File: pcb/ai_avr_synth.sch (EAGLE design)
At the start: 50 parts, among them IC1 ATMEGA328P-PDIP, J1 1X02ST, J2 1X06, J3 1X08, J4 1X08, J5 MIDIJACK, U1 MC7805, U2 TLC2262, U3 6N138

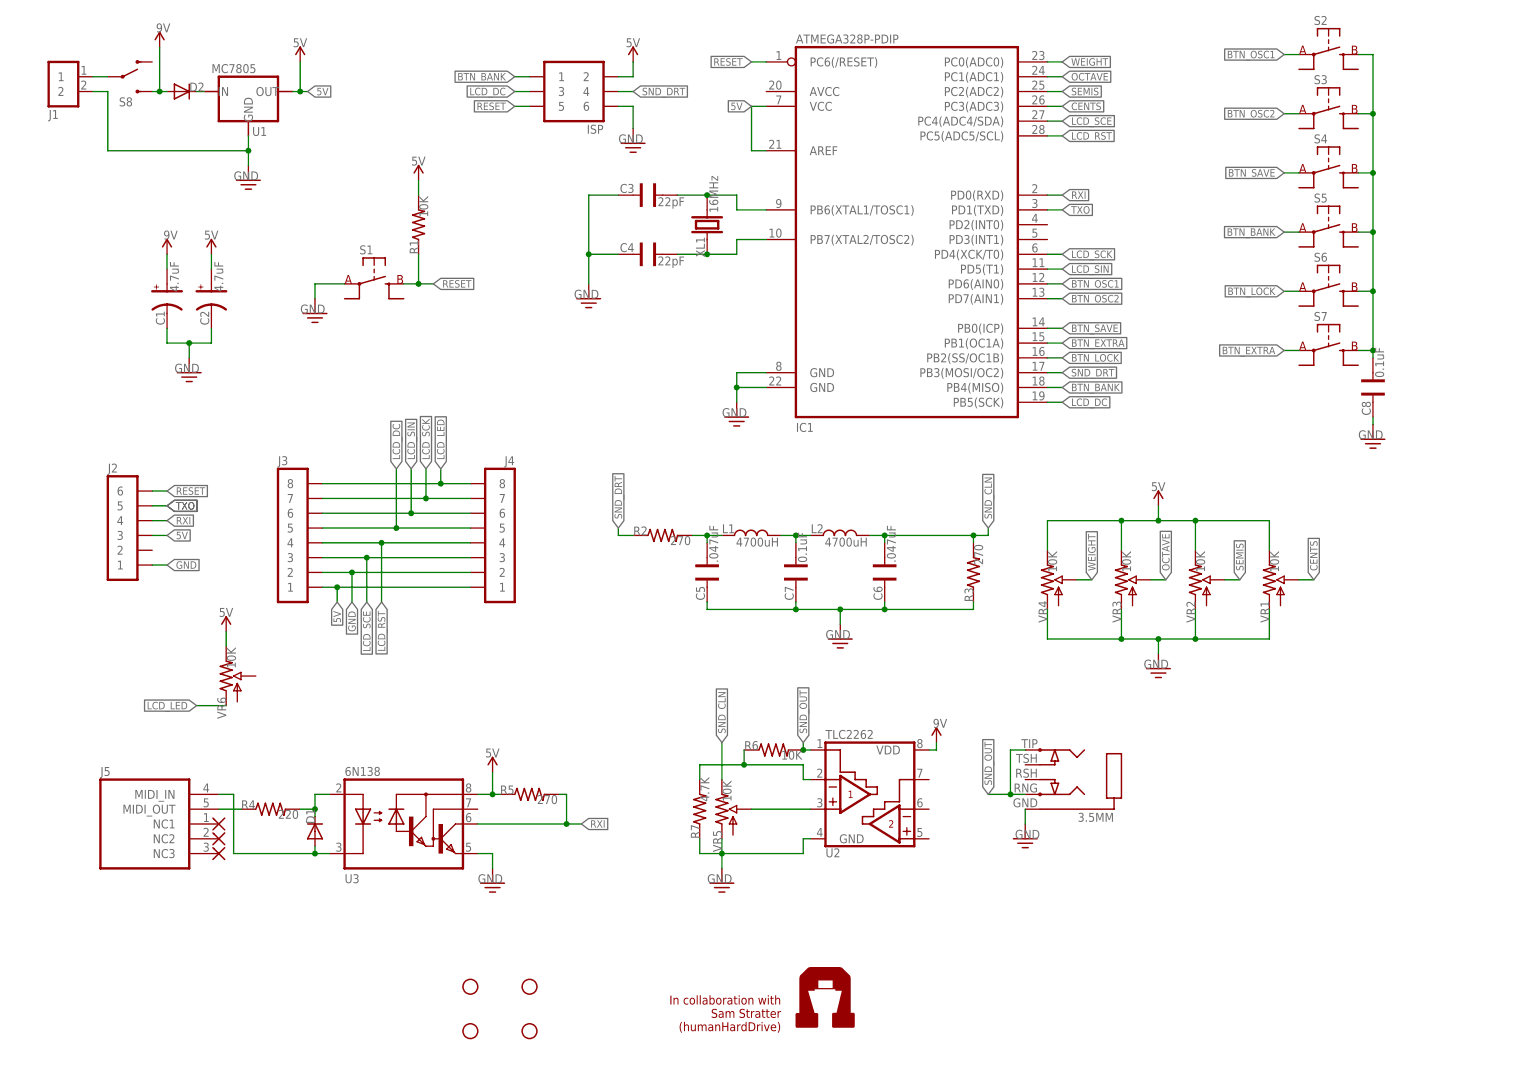
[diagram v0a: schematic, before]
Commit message: updated a few components
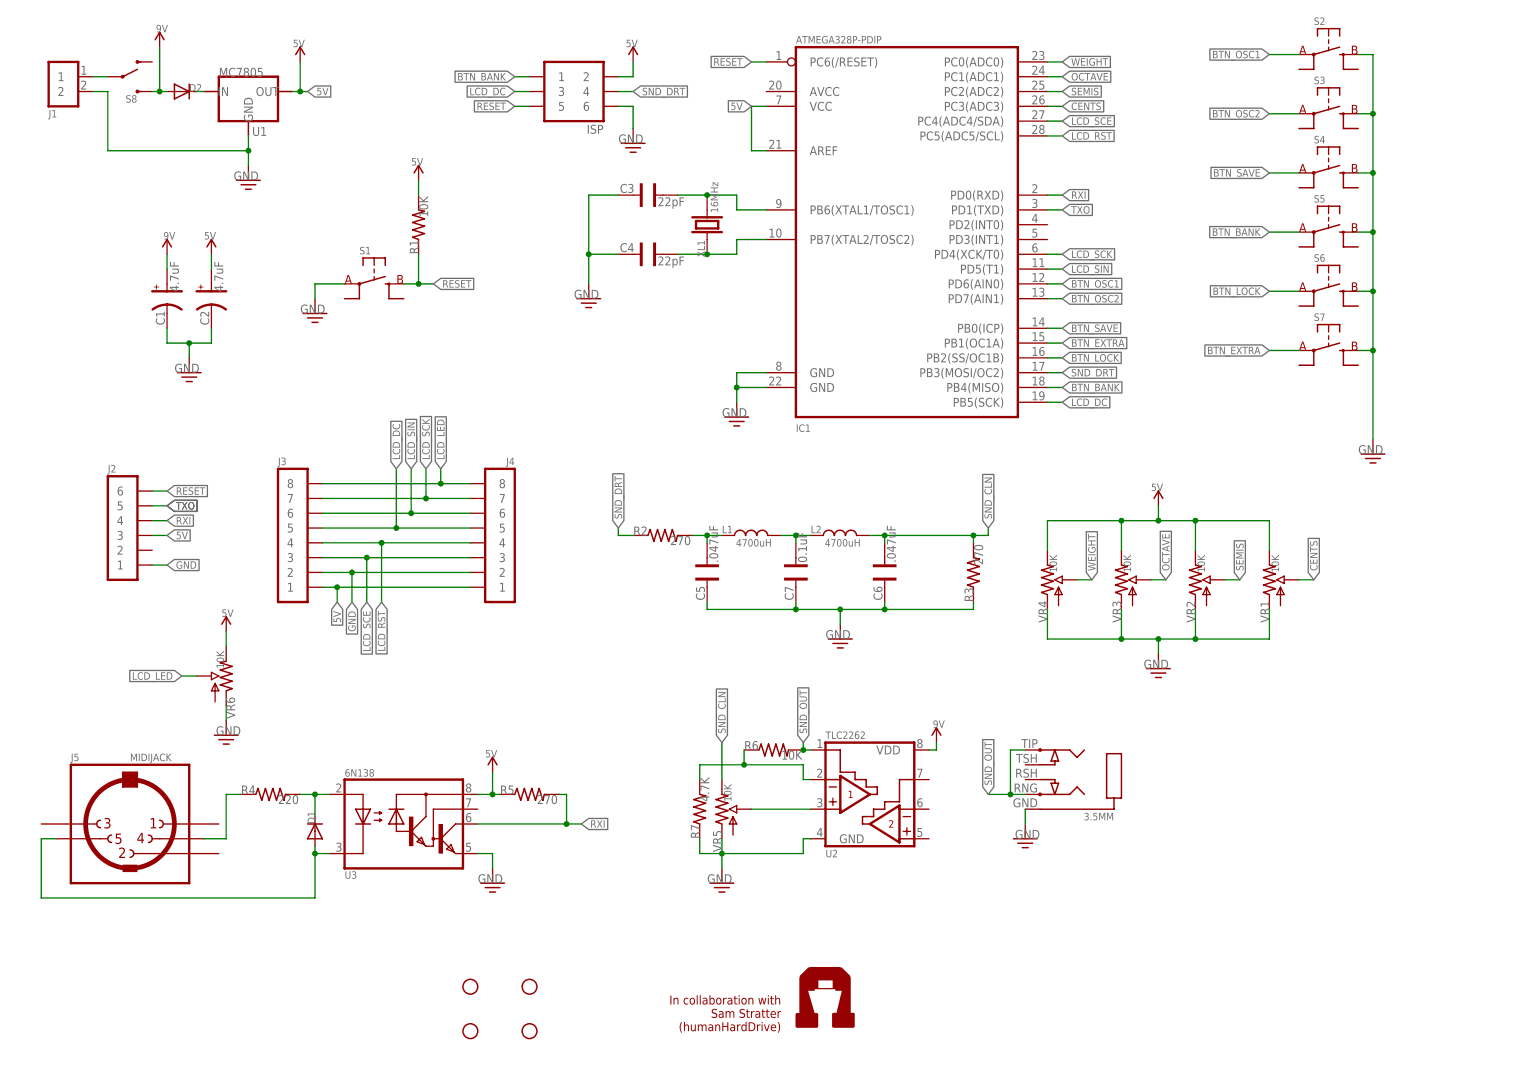
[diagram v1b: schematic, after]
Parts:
- removed C8: 0.1uF, Ai_Passives:CAP025X050
- XL1: device Ai_Passives:CRYSTALHC49S -> Ai_FrequencyControl:CRYSTALHC49S
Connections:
- removed net N$2: C8.1, S2.B@1, S3.B@1, S4.B@1, S5.B@1, S6.B@1, S7.B@1
- net GND: now also S2.B@1, S3.B@1, S4.B@1, S5.B@1, S6.B@1, S7.B@1, VR6.A; no longer C8.2
- net LCD_LED: now also VR6.S; no longer VR6.A
- net N$1: now also J5.4; no longer J5.MIDI_OUT
- net N$10: now also J5.5; no longer J5.MIDI_IN
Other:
- moved on the sheet: R4, VR6

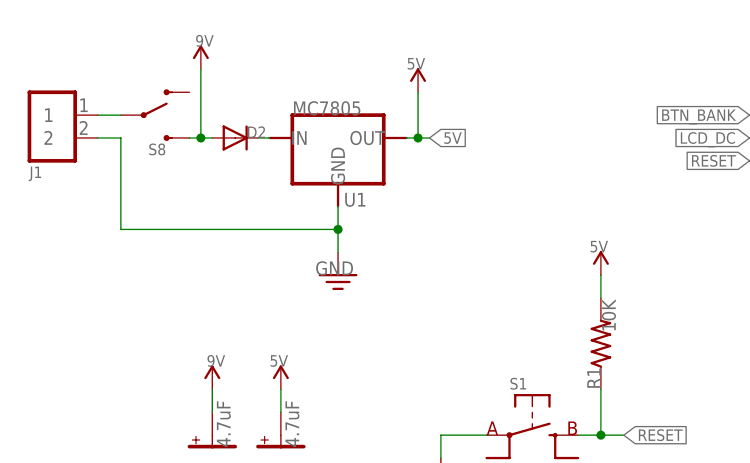
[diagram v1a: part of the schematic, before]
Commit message: fixed trimmer footprint
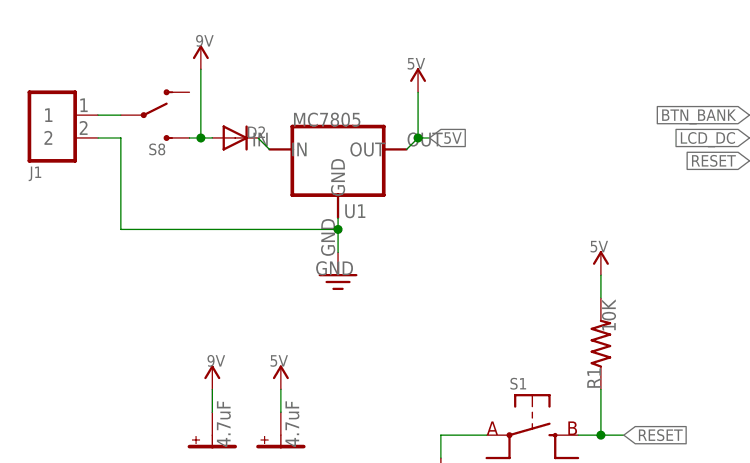
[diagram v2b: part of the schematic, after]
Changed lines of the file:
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@@
 <pinref part="GND1" gate="GND" pin="GND"/>
 <wire x1="40.64" y1="153.67" x2="40.64" y2="156.21" width="0.1524" layer="91"/>
-<wire x1="40.64" y1="156.21" x2="40.64" y2="158.75" width="0.1524" layer="91"/>
+<wire x1="40.64" y1="156.21" x2="40.64" y2="157.48" width="0.1524" layer="91"/>
 <wire x1="16.51" y1="156.21" x2="40.64" y2="156.21" width="0.1524" layer="91"/>
 <junction x="40.64" y="156.21"/>
@@
 <segment>
 <pinref part="U1" gate="G$1" pin="OUT"/>
-<wire x1="48.26" y1="166.37" x2="49.53" y2="166.37" width="0.1524" layer="91"/>
+<wire x1="48.26" y1="165.1" x2="49.53" y2="166.37" width="0.1524" layer="91"/>
 <wire x1="49.53" y1="166.37" x2="49.53" y2="171.45" width="0.1524" layer="91"/>
 <pinref part="U$2" gate="G$1" pin="5V"/>
@@
 <pinref part="D2" gate="G$1" pin="C"/>
 <pinref part="U1" gate="G$1" pin="IN"/>
-<wire x1="31.75" y1="166.37" x2="33.02" y2="166.37" width="0.1524" layer="91"/>
-</segment>
-</net>
+<wire x1="31.75" y1="166.37" x2="33.02" y2="165.1" width="0.1524" layer="91"/>
+</segment>
+</net>

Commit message: updating
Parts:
- removed J2: 1X06, Ai_Connectors:1X06
- added FTDI: 1X06, Ai_Connectors:1X06
- D1: value (none) -> 1N4148
- D2: value (none) -> 1N4001
- STANDOFF5, STANDOFF6, STANDOFF7, STANDOFF8: value STAND-OFF -> STAND-OFF4; device Ai_Electromechanical:STAND-OFF -> Ai_Electromechanical:STAND-OFF4
- U$5: value AI-LOGOL -> AI-LOGOXS; device Ai_Miscellany:AI-LOGOL -> Ai_Miscellany:AI-LOGOXS
- U1: value MC7805 -> MC7805-HOR; device Ai_Power:MC7805 -> Ai_Power:MC7805-HOR
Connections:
- net 5V: now also FTDI.3; no longer J2.3
- net GND: now also FTDI.1; no longer J2.1
- net RESET: now also FTDI.6; no longer J2.6
- net RXI: now also FTDI.4; no longer J2.4
- net TXO: now also FTDI.5; no longer J2.5
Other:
- note removed: "In collaboration with Sam Stratter (humanHardDrive)"
- moved on the sheet: 3.5MM, C1, C2, C3, C4, C5, C6, C7, D1, D2, ISP, J1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

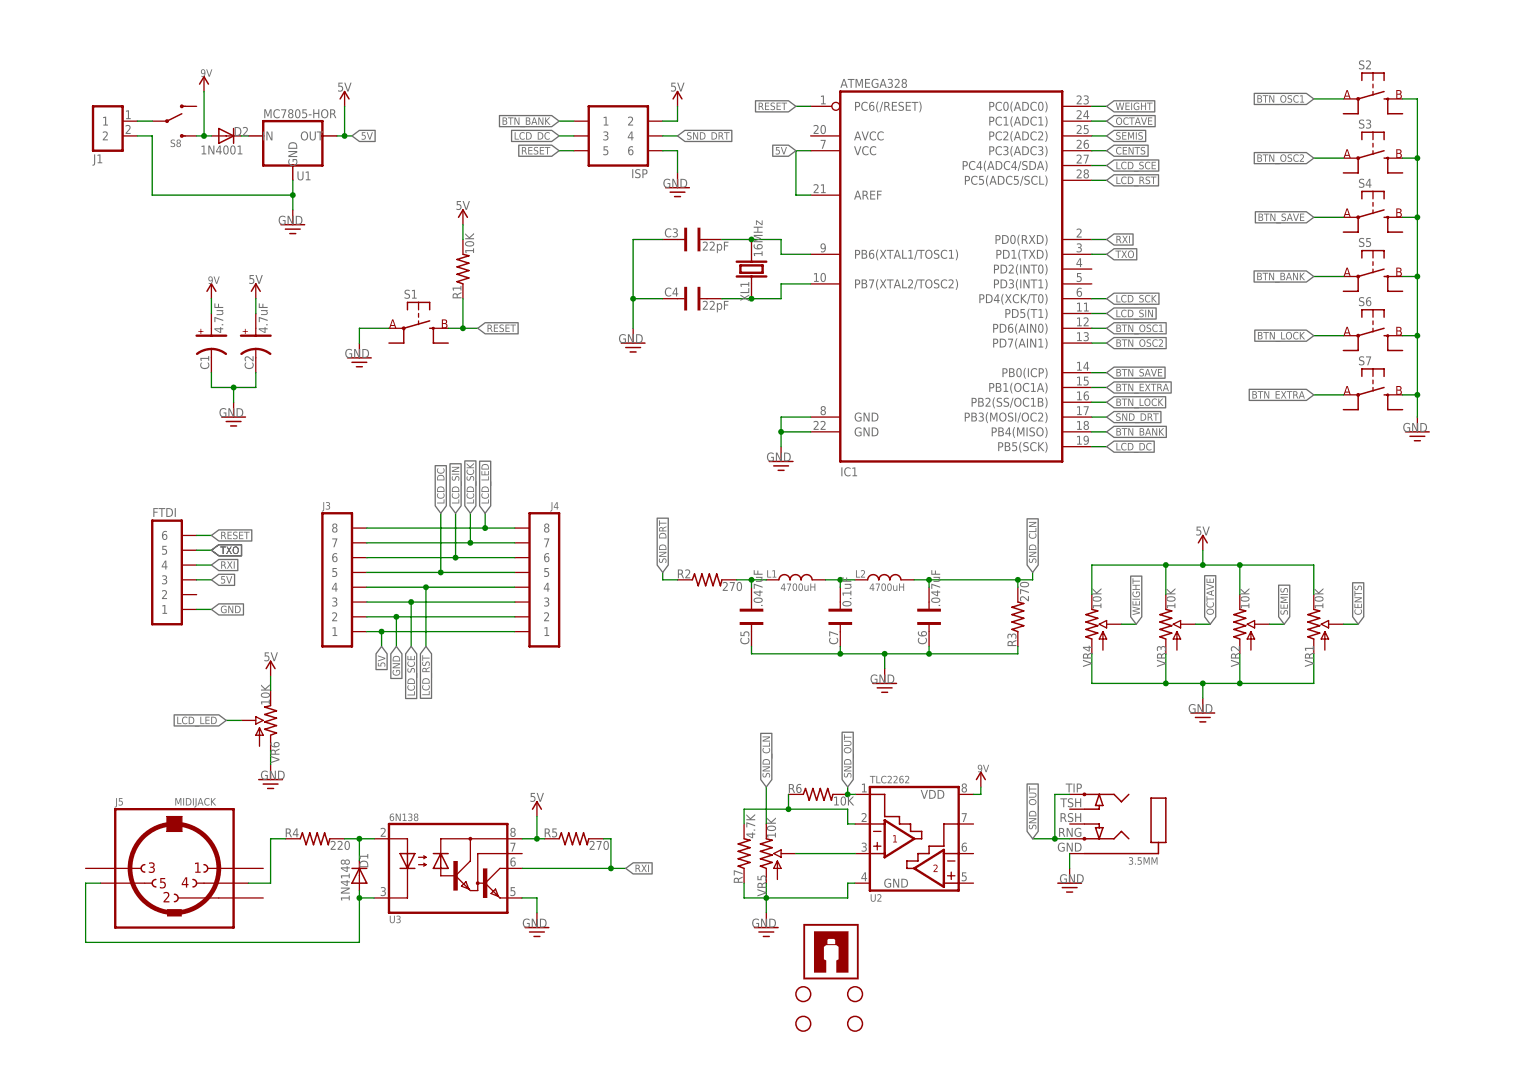
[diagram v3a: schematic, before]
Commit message: adding additional licensing information
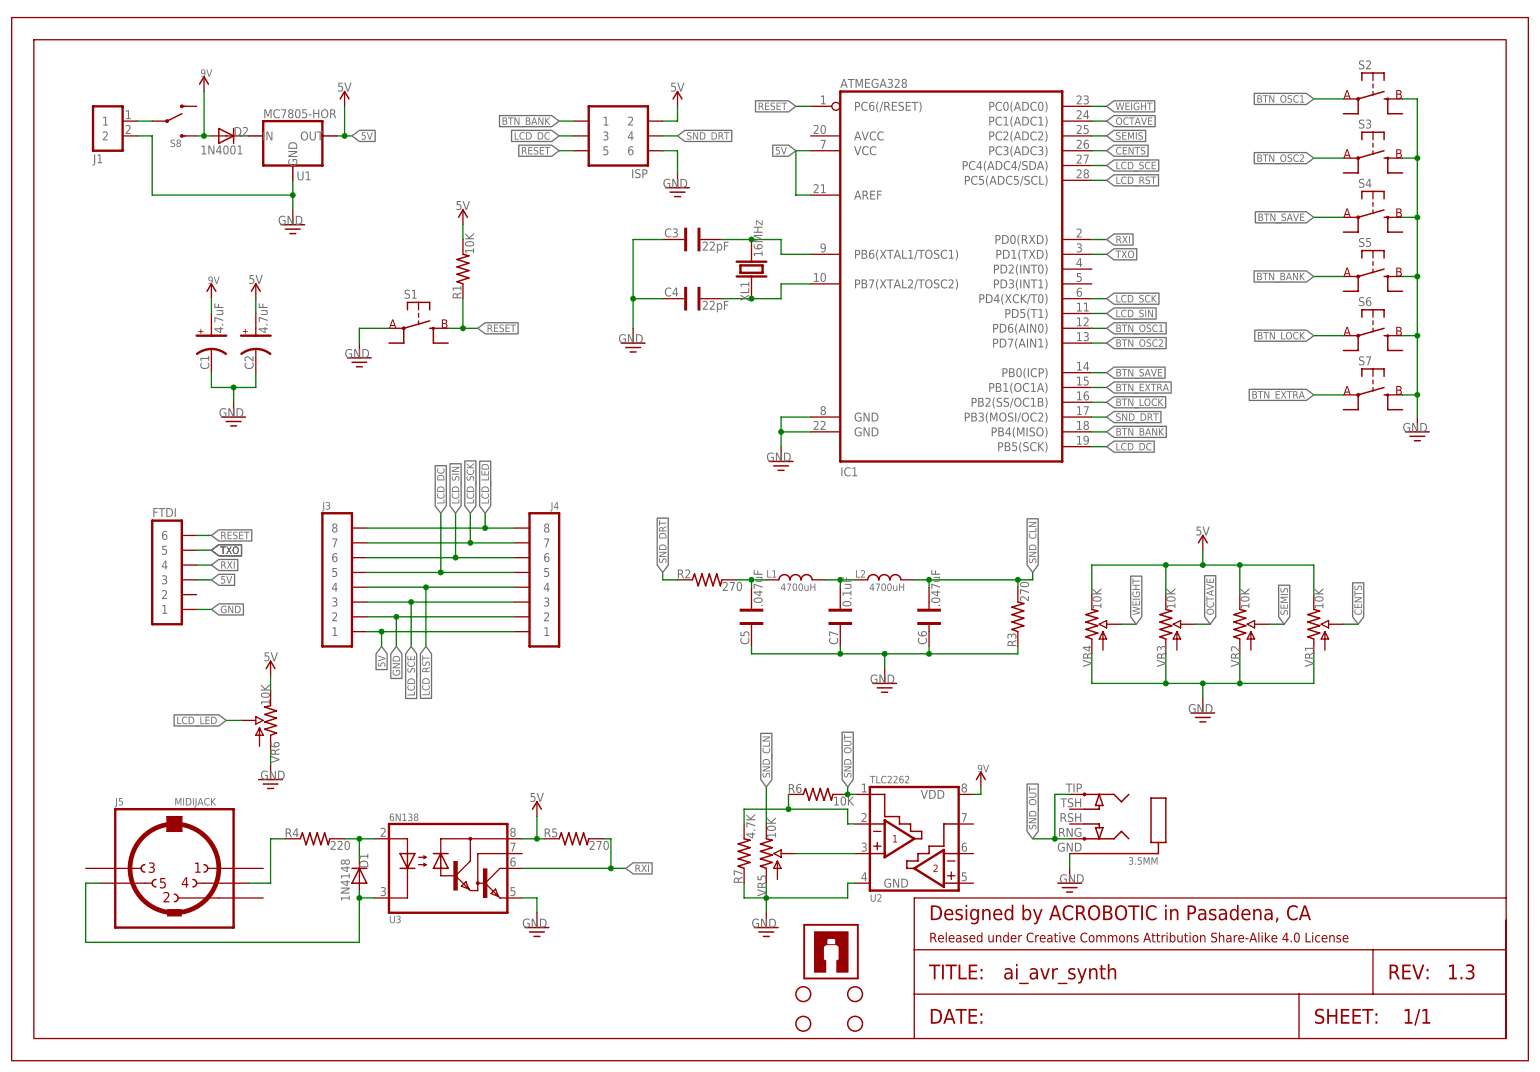
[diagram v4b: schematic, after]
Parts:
- added FRAME1: FRAME-LETTER, Ai_Miscellany:FRAME-LETTER
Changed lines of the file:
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@@
 <?xml version="1.0" encoding="utf-8"?>
 <!DOCTYPE eagle SYSTEM "eagle.dtd">
-<eagle version="6.5.0">
+<eagle version="7.1.0">
 <drawing>
 <settings>
@@
 <parts>
 <part name="FRAME1" library="Ai_Miscellany" deviceset="FRAME-LETTER" device="">
-<attribute name="AUTHOR" value="A.I. HARDWARE SITH LORDS"/>
 <attribute name="REV" value="1.3"/>
 </part>
@@
 </schematic>
 </drawing>
+<compatibility>
+<note version="6.3" minversion="6.2.2" severity="warning">
+Since Version 6.2.2 text objects can contain more than one line,
+which will not be processed correctly with this version.
+</note>
+</compatibility>
 </eagle>

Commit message: updating
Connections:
- net RXI renamed TXD
- net TXO renamed RXD
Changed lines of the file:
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@@
 <?xml version="1.0" encoding="utf-8"?>
 <!DOCTYPE eagle SYSTEM "eagle.dtd">
-<eagle version="7.1.0">
+<eagle version="6.5.0">
 <drawing>
 <settings>
@@
 </segment>
 </net>
-<net name="RXI" class="0">
+<net name="TXD" class="0">
 <segment>
 <pinref part="IC1" gate="G$1" pin="PD0(RXD)"/>
@@
 </segment>
 </net>
-<net name="TXO" class="0">
+<net name="RXD" class="0">
 <segment>
 <pinref part="IC1" gate="G$1" pin="PD1(TXD)"/>
